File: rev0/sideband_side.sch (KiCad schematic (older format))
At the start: 12 parts, among them IC1 ECP5-BGA256, U8 USB3343

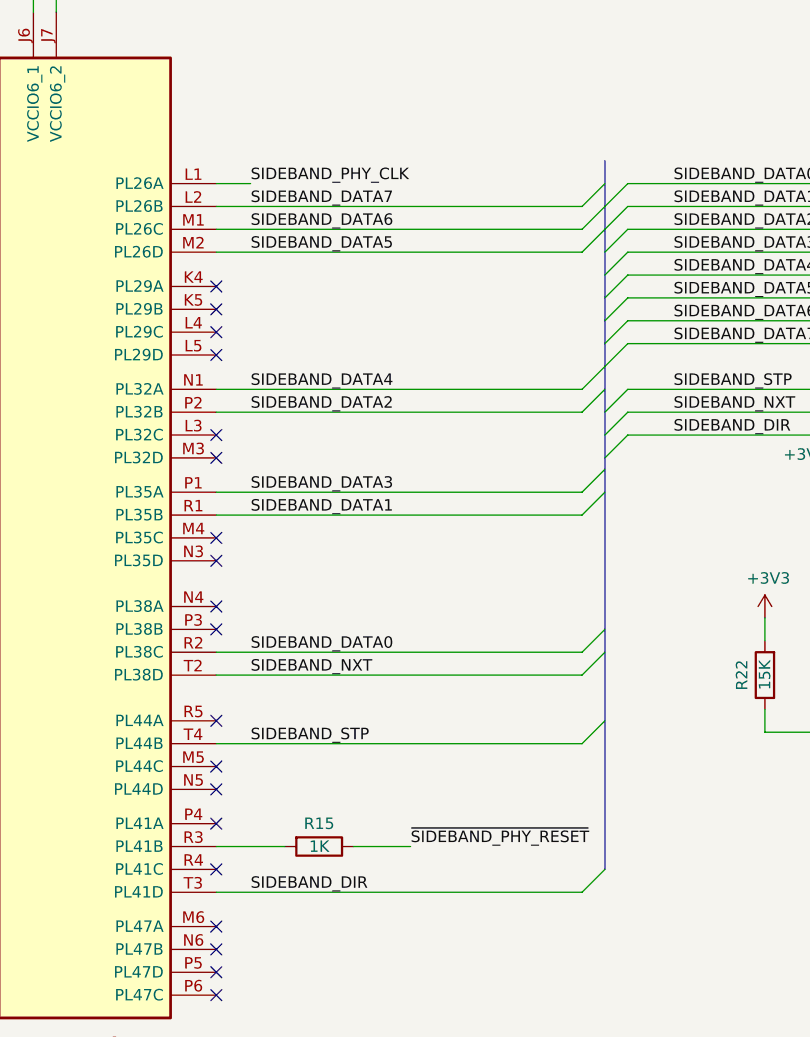
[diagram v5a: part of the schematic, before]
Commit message: rev0: get most of the major routing done
still needs power routing, length matching for the busses,
and routing for the misc control stuff
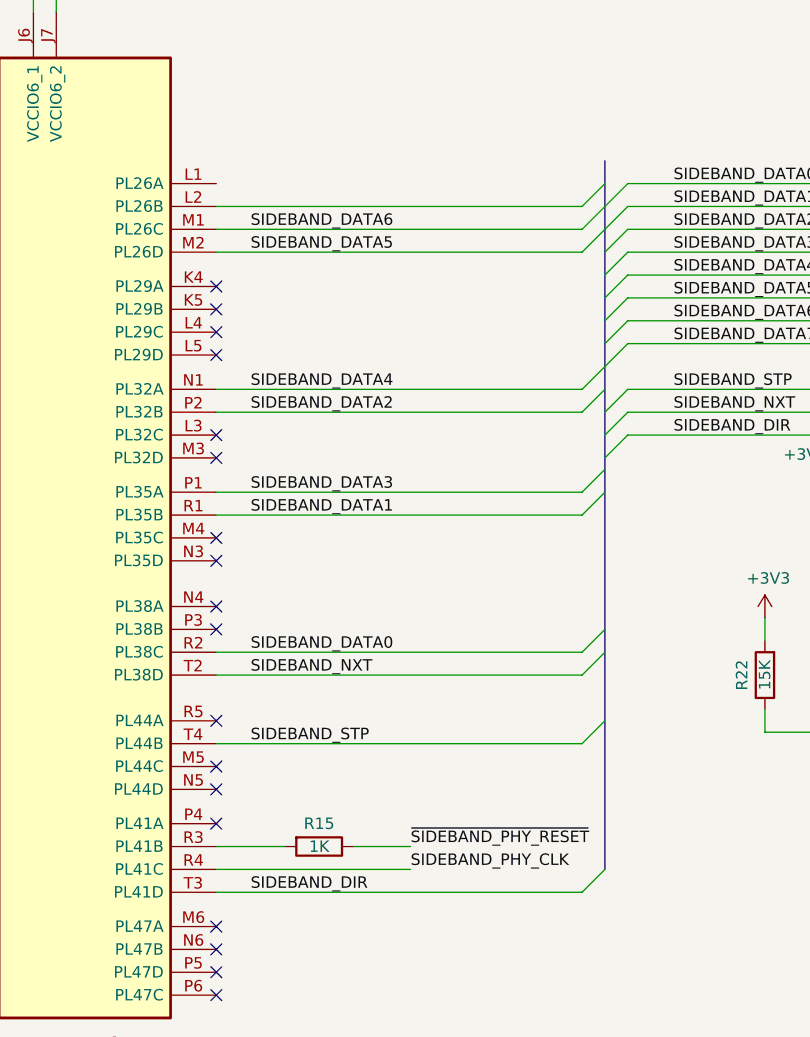
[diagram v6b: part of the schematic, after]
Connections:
- net SIDEBAND_DATA7: no longer IC1.L2 (PL26B)
- net SIDEBAND_PHY_CLK: now also IC1.R4 (PL41C); no longer IC1.L1 (PL26A)
- no-connect marks 20 -> 19
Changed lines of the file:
@@
 Text Label 7650 3700 2    50   ~ 0
-SIDEBAND_PHY_CLK
-Text Label 2650 2450 0    50   ~ 0
 SIDEBAND_PHY_CLK
 Text Label 4500 2850 0    50   ~ 0
@@
 NoConn ~ 2500 5100
 NoConn ~ 2500 5250
-NoConn ~ 2500 5450
 NoConn ~ 2500 5700
 NoConn ~ 2500 5800
@@
 Text Label 2650 3900 0    50   ~ 0
 SIDEBAND_DATA1
+Text Label 3350 5450 0    50   ~ 0
+SIDEBAND_PHY_CLK
 Text Label 2650 3450 0    50   ~ 0
 SIDEBAND_DATA2
@@
 Text Label 2650 2650 0    50   ~ 0
 SIDEBAND_DATA6
-Text Label 2650 2550 0    50   ~ 0
-SIDEBAND_DATA7
-Wire Wire Line
-	2500 2450 2650 2450
+Wire Wire Line
+	3350 5450 2500 5450
 Wire Bus Line
 	4200 2350 4200 5450

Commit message: rev0: routing: get our routing significnatly more complete :)
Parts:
- removed TP5, TP6: TestPoint, TestPoint:TestPoint_Pad_1.0x1.0mm, symbol Connector:TestPoint
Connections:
- net SIDEBAND_DATA7: now also IC1.L2 (PL26B)
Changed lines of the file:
@@
 Wire Wire Line
 	7150 4500 7150 4350
-Wire Wire Line
-	6750 4050 6800 4050
 $Comp
 L Device:C C37
@@
 	7600 4050 7600 3950
 Connection ~ 7600 3950
-Wire Wire Line
-	7600 3950 7850 3950
-$Comp
-L Connector:TestPoint TP6
-U 1 1 5DD2BF2B
-P 7900 3800
-F 0 "TP6" V 7855 3987 50  0000 L CNN
-F 1 "TestPoint" V 7945 3987 50  0000 L CNN
-F 2 "TestPoint:TestPoint_Pad_1.0x1.0mm" H 8100 3800 50  0001 C CNN
-F 3 "~" H 8100 3800 50  0001 C CNN
-	1    7900 3800
-	0    1    1    0
-$EndComp
-Wire Wire Line
-	7900 3800 7850 3800
-Wire Wire Line
-	7850 3800 7850 3950
-Connection ~ 7850 3950
-Wire Wire Line
-	7850 3950 8050 3950
-$Comp
-L Connector:TestPoint TP5
-U 1 1 5DD2DA1C
-P 6800 4250
-F 0 "TP5" H 6850 4500 50  0000 R CNN
-F 1 "TestPoint" H 7000 4600 50  0000 R CNN
-F 2 "TestPoint:TestPoint_Pad_1.0x1.0mm" H 7000 4250 50  0001 C CNN
-F 3 "~" H 7000 4250 50  0001 C CNN
-	1    6800 4250
-	-1   0    0    1
-$EndComp
-Wire Wire Line
-	6800 4250 6800 4050
-Connection ~ 6800 4050
-Wire Wire Line
-	6800 4050 7150 4050
 Text HLabel 7450 2850 2    50   Input ~ 0
 SIDEBAND_VBUS
@@
 Wire Wire Line
 	3350 5450 2500 5450
+Text Label 2650 2550 0    50   ~ 0
+SIDEBAND_DATA7
+Wire Wire Line
+	7600 3950 8050 3950
 Wire Bus Line
 	4200 2350 4200 5450
+Wire Wire Line
+	6750 4050 7150 4050
 $EndSCHEMATC
